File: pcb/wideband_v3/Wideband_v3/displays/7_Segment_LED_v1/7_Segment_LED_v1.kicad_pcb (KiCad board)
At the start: 4 copper layers, 80 x 50 mm, 30 parts, among them J1 Conn_01x10, U1 4511, U10 74AUC2G04, U2 SM420561N, U3 SM420561N, U4 4511, U5 4511, U6 4511, U7 SM420561N, U8 SM420561N

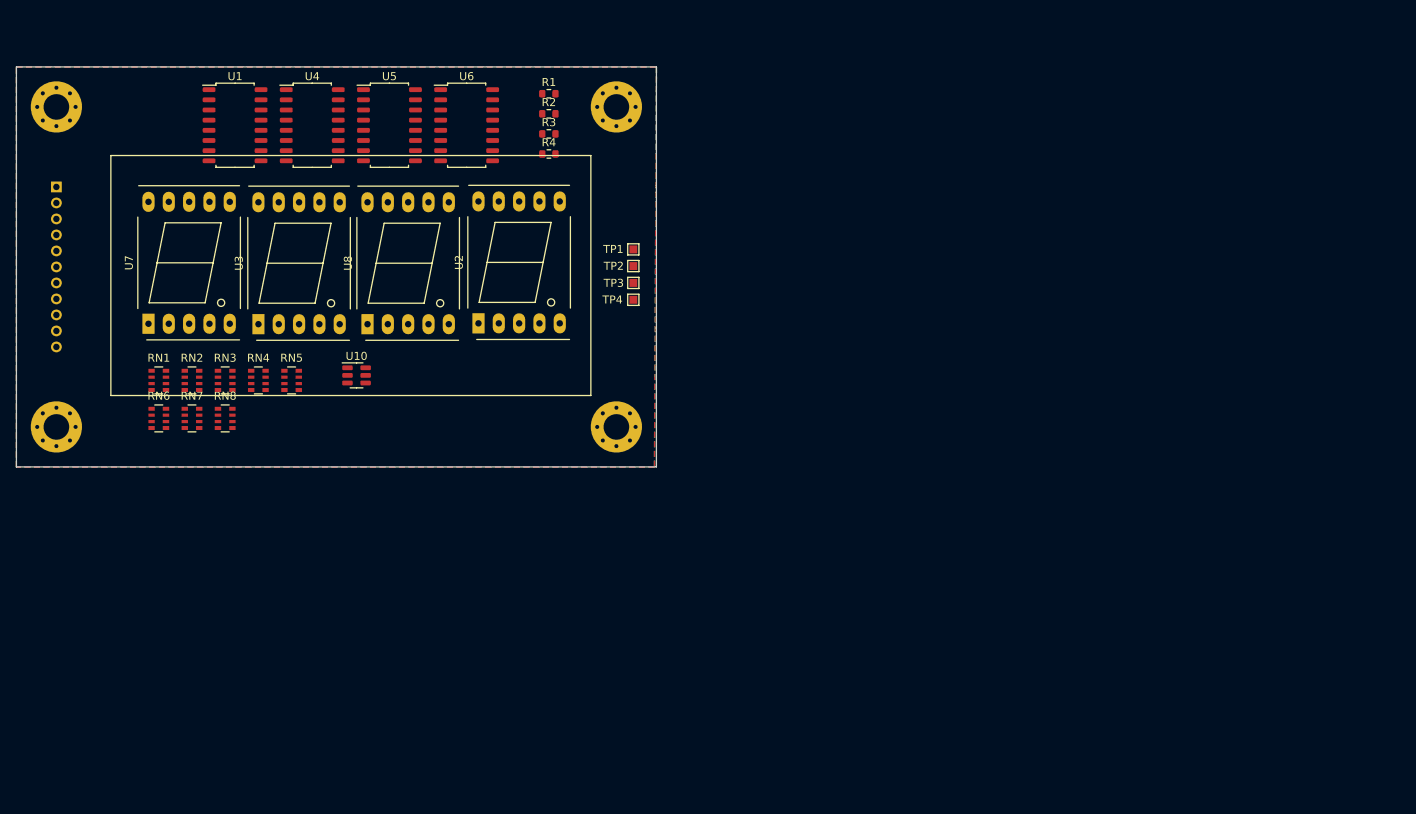
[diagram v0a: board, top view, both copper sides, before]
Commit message: rev3, reduce extended component count
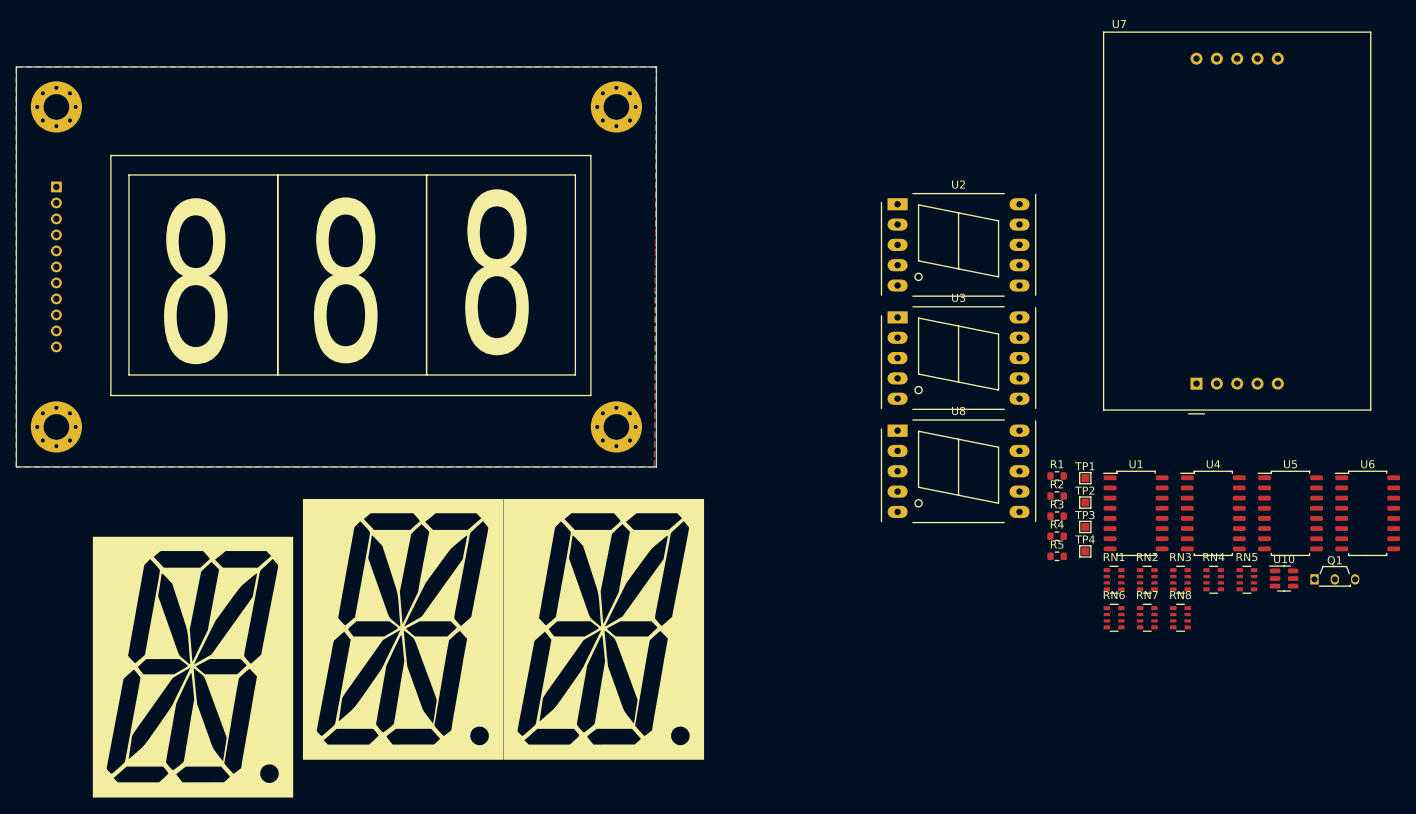
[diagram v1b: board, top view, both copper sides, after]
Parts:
- added G***: LOGO, LOGO, F.Cu at (179.1, 141.4)
- added G***: LOGO, LOGO, F.Cu at (127.7, 146.2)
- added G***: LOGO, LOGO, F.Cu at (154.0, 141.4)
- added Q1: BC847, Package_TO_SOT_THT:TO-92S_Wide, F.Cu at (267.9, 135.2)
- added R5: 10k, Resistor_SMD:R_0603_1608Metric, F.Cu at (235.7, 132.3)
- U7: footprint Display_7Segment:7SegmentLED_LTS6760_LTS6780 -> Display_7Segment:SA15-11xxx
- moved U7 131.2 mm to (253.2, 110.7)
- moved U1 122.6 mm to (245.6, 126.9)
- moved U4 122.6 mm to (255.3, 126.9)
- moved U5 122.6 mm to (264.9, 126.9)
- moved U6 122.6 mm to (274.6, 126.9)
- moved RN2 122.0 mm to (247.0, 135.2)
- moved RN7 122.0 mm to (247.0, 140.0)
- moved RN1 122.0 mm to (242.9, 135.2)
- moved RN3 122.0 mm to (251.2, 135.2)
- moved RN4 122.0 mm to (255.3, 135.2)
- moved RN6 122.0 mm to (242.9, 140.0)
- moved RN8 122.0 mm to (251.2, 140.0)
- moved RN5 122.0 mm to (259.5, 135.2)
- moved U10 118.7 mm to (264.1, 135.1)
- moved U3 79.9 mm to (215.8, 102.4), turned to 0 degrees
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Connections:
- RN1 pad 4: +5V -> Net-(Q1-E)
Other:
- board text added: "8"

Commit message: update 7seg footprint
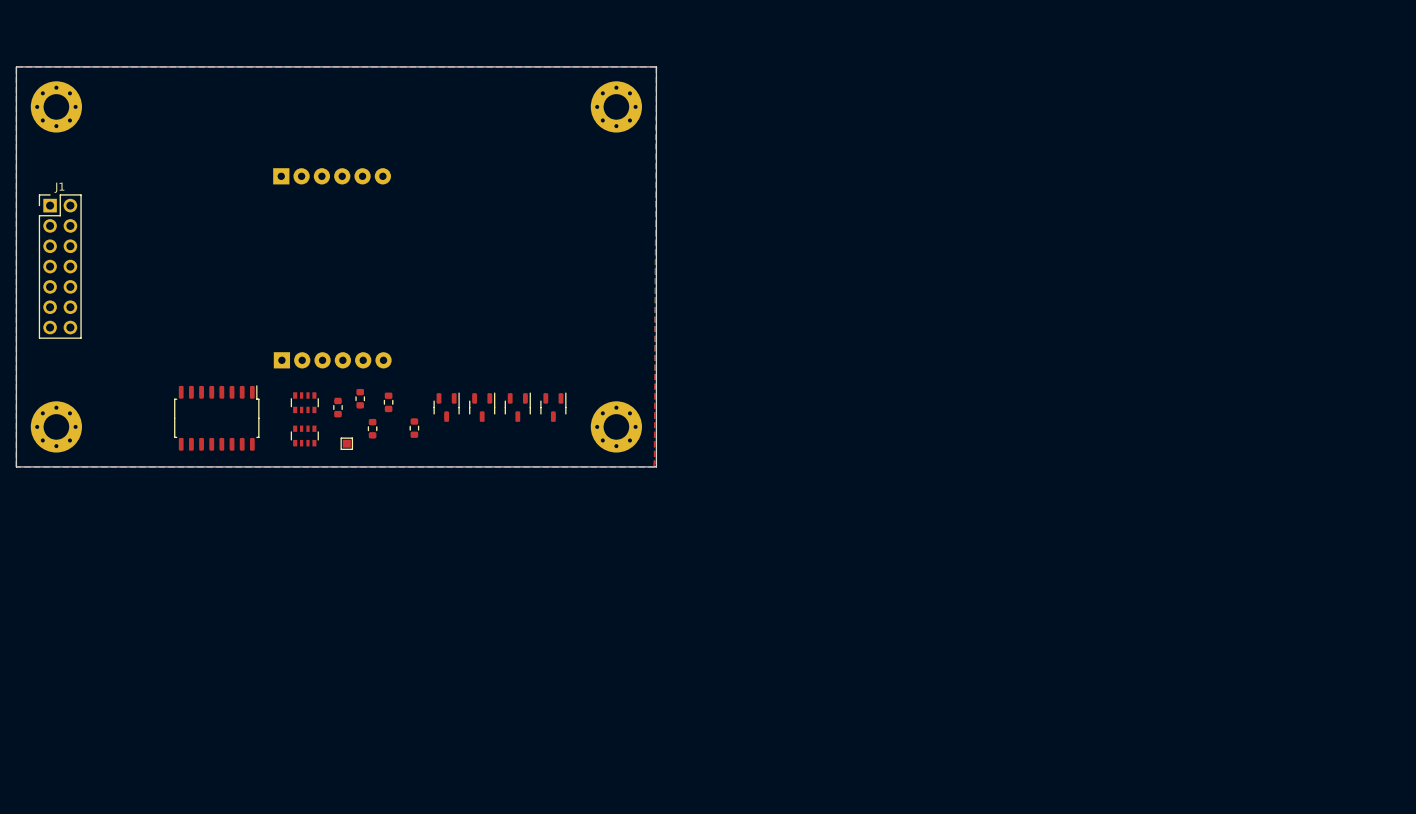
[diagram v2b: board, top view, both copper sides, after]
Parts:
- removed G*** (x3): LOGO, LOGO
- removed RN1, RN2, RN3, RN4, RN7, RN8: 1K, Resistor_SMD:R_Array_Convex_4x0603
- removed TP1, TP2, TP4: TestPoint, TestPoint:TestPoint_Pad_1.0x1.0mm
- removed U10: 74AUC2G04, Package_TO_SOT_SMD:SOT-23-6
- removed U2, U3, U8: SM420561N, Display_7Segment:7SegmentLED_LTS6760_LTS6780
- removed U4, U6: 4511, Package_SO:SOP-16_4.55x10.3mm_P1.27mm
- removed U7: SM420561N, Display_7Segment:SA15-11xxx
- added Q2: BC847, Package_TO_SOT_SMD:SOT-23-3, F.Cu at (168.3, 113.7)
- added Q3: BC847, Package_TO_SOT_SMD:SOT-23-3, F.Cu at (163.9, 113.7)
- added Q4: BC847, Package_TO_SOT_SMD:SOT-23-3, F.Cu at (159.4, 113.7)
- J1: value Conn_01x10 -> Conn_01x14; footprint Connector_PinSocket_2.00mm:PinSocket_1x11_P2.00mm_Vertical -> Connector_PinHeader_2.54mm:PinHeader_2x07_P2.54mm_Vertical; moved to F.Cu
- Q1: footprint Package_TO_SOT_THT:TO-92S_Wide -> Package_TO_SOT_SMD:SOT-23-3
- U1: value 4511 -> ~; footprint Package_SO:SOP-16_4.55x10.3mm_P1.27mm -> Library:LED_7SEG
- moved U5 134.7 mm to (130.7, 115.0), turned to -90 degrees
- moved RN5 119.8 mm to (141.7, 113.1), turned to -90 degrees
- moved U1 105.2 mm to (145.3, 95.3)
- moved RN6 103.7 mm to (141.7, 117.2), turned to -90 degrees
- moved Q1 97.5 mm to (172.8, 113.7), turned to -90 degrees
- moved TP3 92.9 mm to (147.0, 118.2), turned to -90 degrees
- moved R2 90.6 mm to (145.9, 113.7), turned to -90 degrees
- moved R1 87.6 mm to (148.6, 112.6), turned to -90 degrees
- moved R4 86.6 mm to (150.2, 116.3), turned to -90 degrees
- moved R3 84.8 mm to (152.2, 113.0), turned to -90 degrees
- moved R5 81.9 mm to (155.4, 116.3), turned to -90 degrees
- moved J1 2.46 mm to (109.9, 88.5), turned to 0 degrees
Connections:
- J1 pad 10: +3V3 -> /SEG_2
- J1 pad 11: +5V -> /SEG_1
- J1 pad 2: /DP_SEG_2 -> unconnected-(J1-Pin_2-Pad2)
- J1 pad 3: /PWM -> /DP_SEG
- J1 pad 4: /DD -> /PWM
- J1 pad 5: /DC -> /DD
- J1 pad 6: /DB -> /DC
- J1 pad 7: /DA -> /DB
- J1 pad 8: /ENABLE_B -> /DA
- J1 pad 9: /ENABLE_A -> /SEG_3
- R1 pad 1: +5V -> /SEG_1
- R2 pad 1: +5V -> /SEG_2
- R2 pad 2: Net-(U1-~{LT}) -> Net-(Q3-B)
- R4 pad 1: +5V -> /DP_SEG
- R4 pad 2: Net-(U6-~{LT}) -> Net-(Q1-B)
- R5 pad 1: /DP_SEG_2 -> /SEG_3
- R5 pad 2: Net-(Q1-B) -> Net-(Q4-B)
- RN6 pad 4: unconnected-(RN6-R4.1-Pad4) -> Net-(Q1-E)
- U1 pad 1: /DB -> Net-(RN6-R1.2)
- U1 pad 10: Net-(RN3-R4.1) -> Net-(RN6-R2.2)
- U1 pad 11: Net-(RN3-R3.1) -> Net-(RN5-R1.2)
- U1 pad 2: /DC -> Net-(RN5-R4.2)
- U1 pad 3: Net-(U1-~{LT}) -> Net-(RN6-R4.2)
- U1 pad 4: /PWM -> Net-(RN5-R3.2)
- U1 pad 5: /ENABLE_4 -> Net-(RN6-R3.2)
- U1 pad 6: /DD -> (no net)
- U1 pad 7: /DA -> Net-(RN5-R2.2)
- U1 pad 8: GND -> Net-(Q4-C)
- U5 pad 5: /ENABLE_1 -> /ENABLE
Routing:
- net /DD: track 0.81 -> 0.00 mm
- removed copper zone on In1.Cu, net GND
- removed copper zone on In2.Cu, net GND
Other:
- copper layers 4 -> 2
- board text removed: "8"

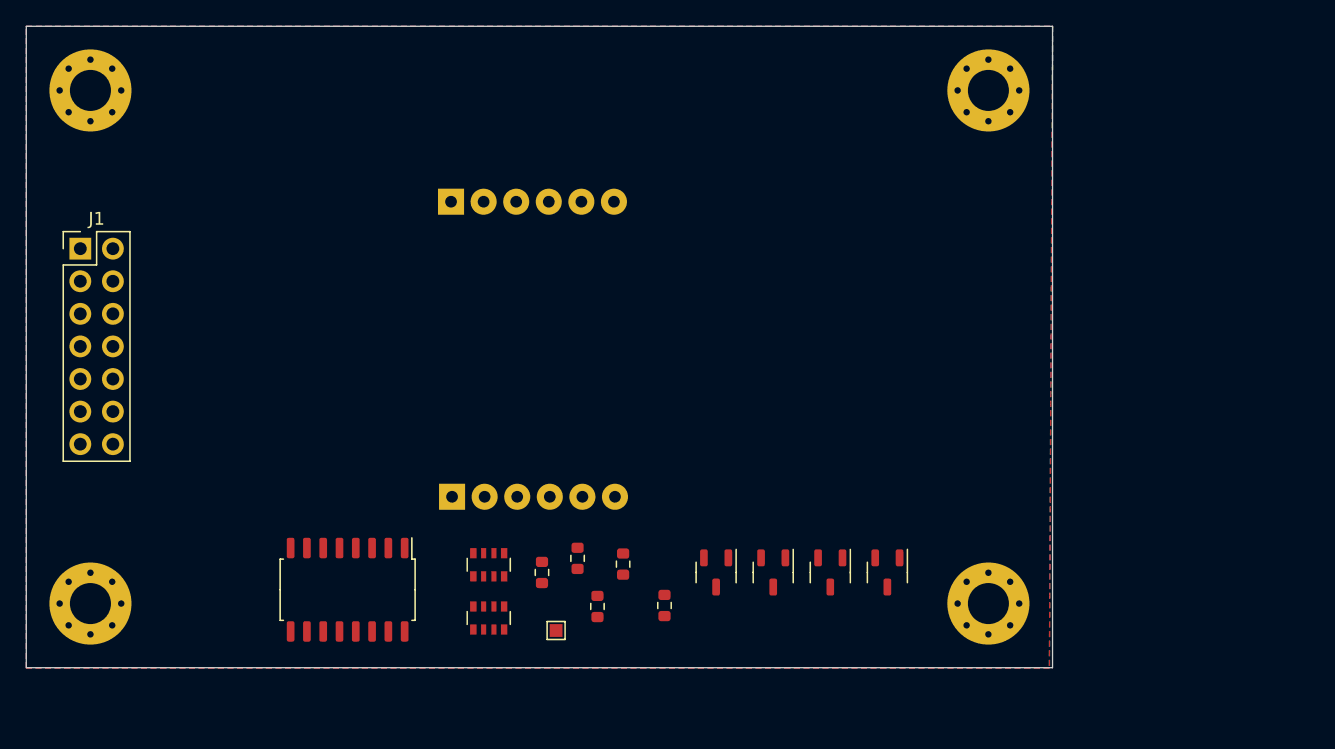
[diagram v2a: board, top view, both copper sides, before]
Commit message: rev3: update connector on main board
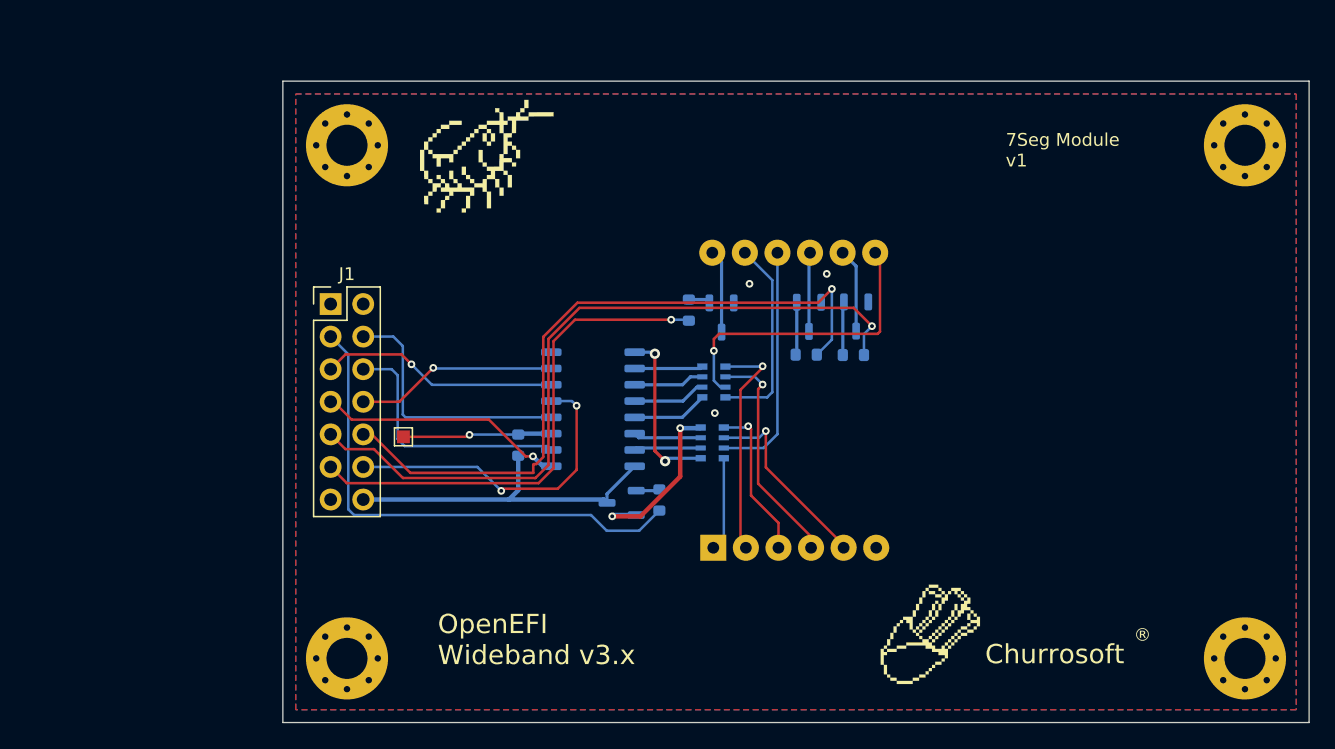
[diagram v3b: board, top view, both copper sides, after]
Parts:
- added G***: LOGO, LOGO, F.Cu at (141.6, 81.4)
- added G***: LOGO, LOGO, F.Cu at (176.3, 118.4)
- added G***: LOGO, LOGO, B.Cu at (160.0, 94.6)
- added G***: LOGO, LOGO, B.Cu at (188.6, 115.1)
- added G***: LOGO, LOGO, B.Cu at (151.3, 113.9)
- Q1, Q2, Q3, Q4, R1, R2, R3, R4, R5, RN5, RN6, U5: moved to B.Cu
- U1: footprint Library:LED_7SEG -> Connector_PinHeader_2.00mm:PinHeader_2x12_P2.00mm_Vertical
- moved R2 26.7 mm to (166.5, 96.7), turned to 180 degrees
- moved R5 24.5 mm to (170.1, 96.7), turned to 180 degrees
- moved U5 23.7 mm to (149.8, 101.0), turned to 0 degrees
- moved Q4 22.7 mm to (170.4, 93.7)
- moved RN5 22.6 mm to (159.3, 98.8), turned to 0 degrees
- moved RN6 22.1 mm to (159.1, 103.6), turned to 0 degrees
- moved Q2 21.6 mm to (159.9, 93.8)
- moved Q1 21.4 mm to (152.1, 108.3), turned to 180 degrees
- moved R1 21.2 mm to (157.3, 93.2), turned to 90 degrees
- moved H1 20.5 mm to (200.7, 80.4)
- moved H4 20.5 mm to (200.7, 120.4)
- moved H2 20.5 mm to (130.7, 80.4)
- moved H3 20.5 mm to (130.7, 120.4)
- moved Q3 20.1 mm to (166.7, 93.8)
- moved J1 20.0 mm to (129.4, 92.8)
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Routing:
- net /SEG_3: track 0.00 -> 58.0 mm, vias 0 -> 1
- net /SEG_2: track 0.00 -> 55.2 mm, vias 0 -> 1
- net /DP_SEG: track 0.00 -> 39.6 mm
- net /SEG_1: track 0.00 -> 39.6 mm, vias 0 -> 1
- net +5V: track 0.00 -> 26.6 mm
- net /ENABLE: track 0.00 -> 25.2 mm, vias 0 -> 2
- net Net-(RN5-R2.2): track 0.00 -> 23.9 mm, vias 0 -> 1
- net /PWM: track 0.00 -> 20.4 mm
- net /DC: track 0.00 -> 20.2 mm
- net /DB: track 0.00 -> 19.3 mm, vias 0 -> 1
- net Net-(RN6-R2.2): track 0.00 -> 18.8 mm
- net /DD: track 0.00 -> 18.7 mm, vias 0 -> 1
- net Net-(RN5-R4.2): track 0.00 -> 17.9 mm, vias 0 -> 1
- net Net-(RN5-R3.2): track 0.00 -> 17.7 mm, vias 0 -> 1
- net /DA: track 0.00 -> 15.8 mm, vias 0 -> 1
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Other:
- board text added: "7Seg Module v1"
- board text added: "Churrosoft"
- board text added: "Diseñado en Argentina"
- board text added: "OpenEFI Wideband v3.x"
- board text added: "®"

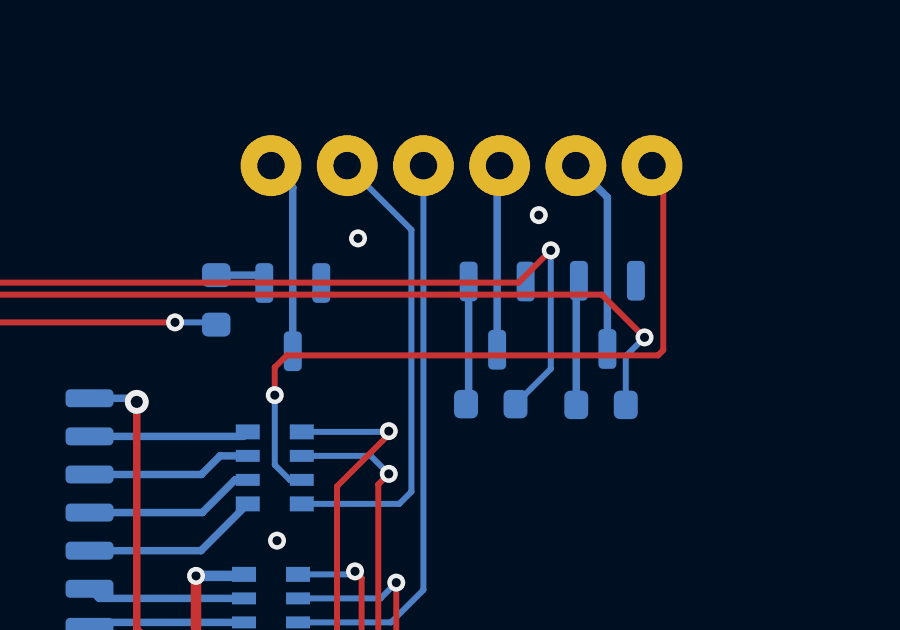
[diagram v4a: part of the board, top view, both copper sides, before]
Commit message: update transistors on rev3
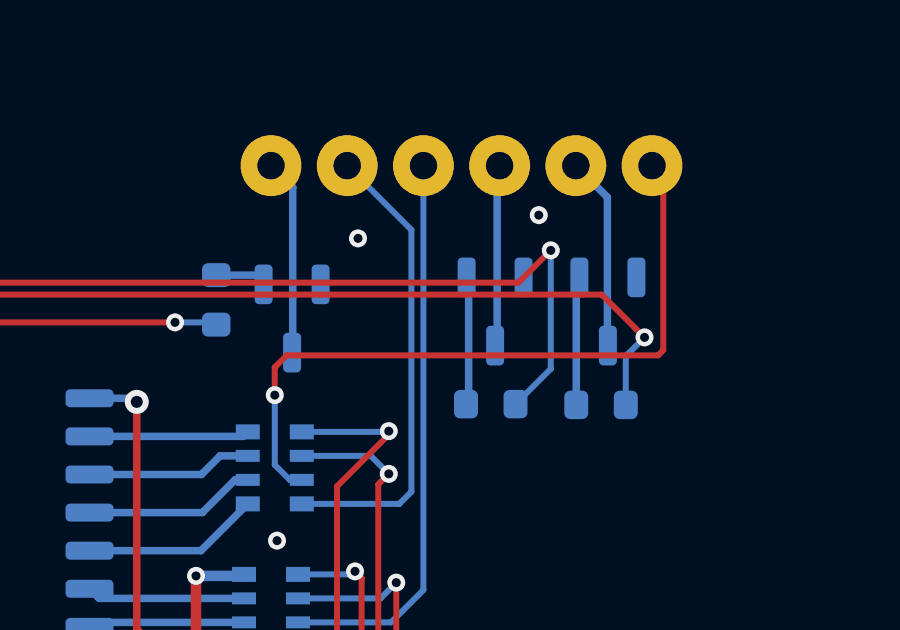
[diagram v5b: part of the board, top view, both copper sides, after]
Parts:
- Q1, Q2, Q3, Q4: value BC847 -> SS8050
- moved Q3 0.15 mm to (166.6, 93.6)
- moved Q4 0.11 mm to (170.4, 93.6)
- moved Q2 0.05 mm to (159.8, 93.9)
